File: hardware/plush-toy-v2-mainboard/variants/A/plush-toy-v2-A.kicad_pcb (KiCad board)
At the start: 4 copper layers, 52 x 46 mm, 99 parts, among them U1 ESP32-S3-WROOM-1-N16R8

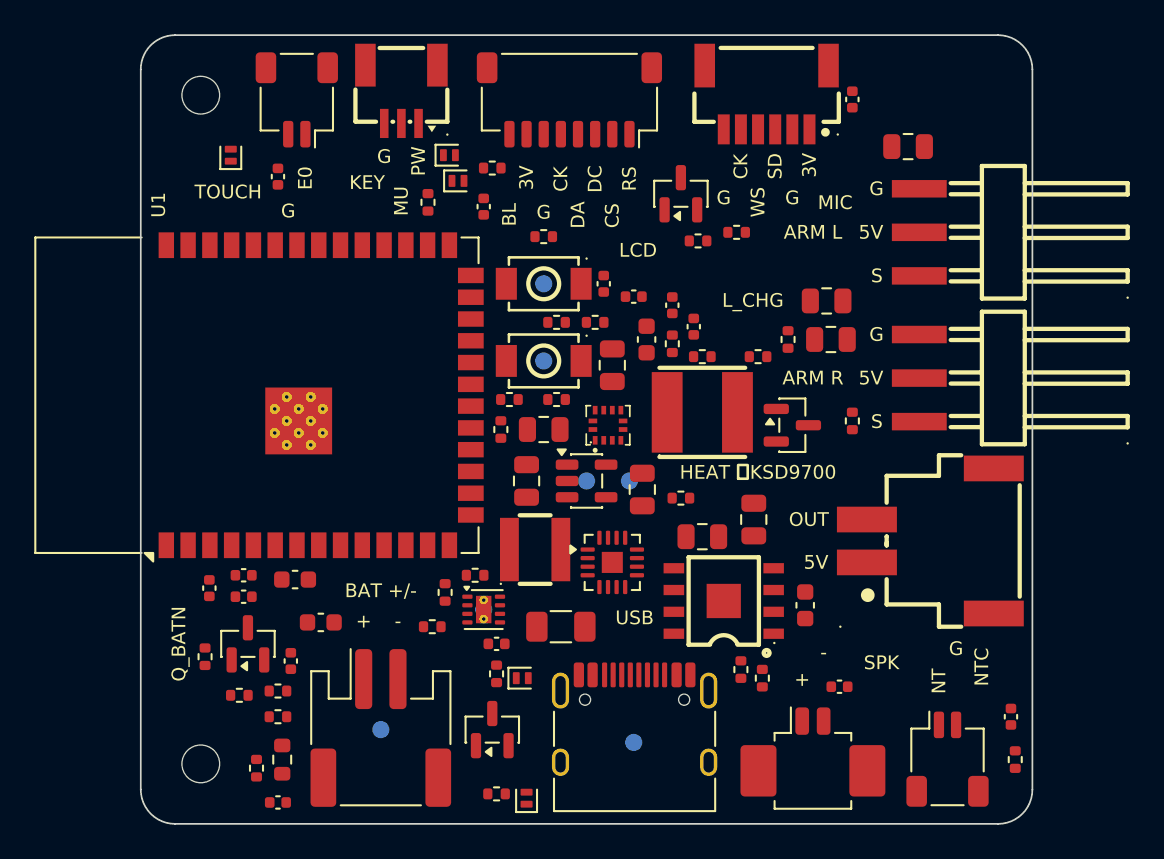
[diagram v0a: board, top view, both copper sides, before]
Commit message: feat(pcb-v2): 版本 A 布线完成，DRC 0 错误 0 未连接
- 网络类收窄（Power 0.6 / Supply 0.4 / Audio 0.3），丝印最小 0.8mm
- In2 改为 VSYS 矩形 + 其余 3V3；电源链按电流走向重排
- IMU SA0 接 3V3（0x19），降压 EN 直连 VSYS
- post_route：网格补线、拉直、快照 --from-snapshot
- route：空 SES 直接失败，非回退只比错误与未连接

Co-Authored-By: Claude Opus 5.5 <noreply@anthropic.com>
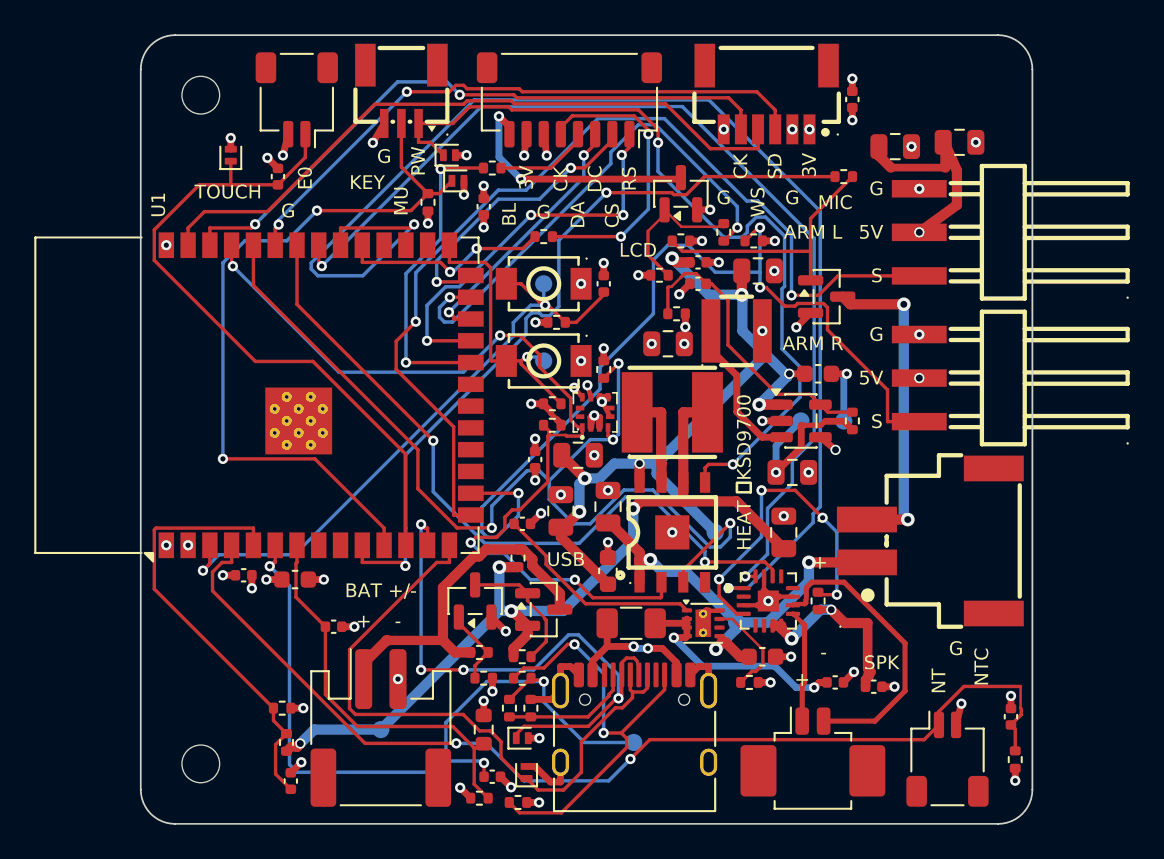
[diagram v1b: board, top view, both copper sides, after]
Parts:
- removed R_BUCK_EN: 100k, Resistor_SMD:R_0402_1005Metric
- moved C_EFUSE_IN 34.9 mm to (40.5, 37.8)
- moved C_VUSB 25.8 mm to (36.2, 36.2)
- moved R_EFUSE_ILM 20.7 mm to (35.5, 37.8), turned to 0 degrees
- moved R_FB1 20.0 mm to (41.5, 22.5), turned to 90 degrees
- moved R_FB2 19.3 mm to (31.2, 16.2)
- moved C_EFUSE_DVDT 18.6 mm to (22.2, 28.5), turned to 0 degrees
- moved L_BUCK 17.3 mm to (34.8, 17.2)
- moved R_BATN_G 16.0 mm to (19.8, 36.0), turned to 0 degrees
- moved R_AMP_SD 15.8 mm to (39.5, 33.0), turned to 90 degrees
- moved R_CC_SUM1 14.9 mm to (21.5, 39.2)
- moved TP_VUSB 14.8 mm to (34.8, 34.2)
- moved C_BUCK_OUT1 14.7 mm to (38.0, 25.5)
- moved R_BATN_PD 14.3 mm to (20.0, 37.5)
- moved Q_BATN 13.5 mm to (19.5, 33.0)
- moved R_BAT_NTC 13.1 mm to (19.8, 44.5), turned to 0 degrees
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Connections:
- J_HEAT pad 3: (no net) -> unconnected-(J_HEAT-Pad3)
- J_HEAT pad 4: (no net) -> unconnected-(J_HEAT-Pad4)
- J_KEY pad 4: (no net) -> unconnected-(J_KEY-Pad4)
- J_KEY pad 5: (no net) -> unconnected-(J_KEY-Pad5)
- J_MIC pad 7: (no net) -> unconnected-(J_MIC-Pad7)
- J_MIC pad 8: (no net) -> unconnected-(J_MIC-Pad8)
- J_USB pad A8: (no net) -> unconnected-(J_USB-SBU1-PadA8)
- J_USB pad B8: (no net) -> unconnected-(J_USB-SBU2-PadB8)
- U1 pad 17: (no net) -> unconnected-(U1-IO9-Pad17)
- U1 pad 18: (no net) -> unconnected-(U1-IO10-Pad18)
- U1 pad 19: (no net) -> unconnected-(U1-IO11-Pad19)
- U1 pad 20: (no net) -> unconnected-(U1-IO12-Pad20)
- U1 pad 21: (no net) -> unconnected-(U1-IO13-Pad21)
- U1 pad 28: (no net) -> unconnected-(U1-IO35-Pad28)
- U1 pad 29: (no net) -> unconnected-(U1-IO36-Pad29)
- U1 pad 30: (no net) -> unconnected-(U1-IO37-Pad30)
- U1 pad 8: (no net) -> unconnected-(U1-IO15-Pad8)
- U1 pad 9: (no net) -> unconnected-(U1-IO16-Pad9)
- U_AMP pad 12: (no net) -> unconnected-(U_AMP-NC-Pad12)
- U_AMP pad 13: (no net) -> unconnected-(U_AMP-NC-Pad13)
- U_AMP pad 2: (no net) -> unconnected-(U_AMP-GAIN_SLOT-Pad2)
- U_AMP pad 5: (no net) -> unconnected-(U_AMP-NC-Pad5)
- U_AMP pad 6: (no net) -> unconnected-(U_AMP-NC-Pad6)
- U_BUCK pad 1: BUCK_EN -> VSYS
- U_CHG pad 4: (no net) -> unconnected-(U_CHG-LED3-Pad4)
- U_EFUSE pad 6: (no net) -> unconnected-(U_EFUSE-FLT-Pad6)
- U_IMU pad 11: (no net) -> unconnected-(U_IMU-INT2-Pad11)
- U_IMU pad 12: (no net) -> unconnected-(U_IMU-INT1-Pad12)
- U_IMU pad 3: GND -> +3V3
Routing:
- net AMP_DIN: track 0.00 -> 75.2 mm, vias 0 -> 2
- net VSYS: track 0.00 -> 73.4 mm, vias 0 -> 12
- net NTC_SENSE: track 0.00 -> 62.0 mm, vias 0 -> 2
- net I2C_SDA: track 0.00 -> 60.7 mm, vias 0 -> 4
- net AMP_BCLK: track 0.00 -> 59.0 mm, vias 0 -> 2
- net SERVO_L_PWM: track 0.00 -> 56.9 mm, vias 0 -> 2
- net GND: track 0.00 -> 54.3 mm, vias 0 -> 58
- net I2C_SCL: track 0.00 -> 54.1 mm, vias 0 -> 4
- net SERVO_R_PWM: track 0.00 -> 53.3 mm, vias 0 -> 3
- net VBAT: track 0.00 -> 51.0 mm, vias 0 -> 4
- net KEY_PWR: track 0.00 -> 48.3 mm, vias 0 -> 2
- net CC_SENSE: track 0.00 -> 45.1 mm, vias 0 -> 3
- net HEAT_GATE_DRV: track 0.00 -> 44.9 mm, vias 0 -> 2
- net KEY_MUTE: track 0.00 -> 43.6 mm, vias 0 -> 2
- net AMP_LRCLK: track 0.00 -> 42.4 mm, vias 0 -> 2
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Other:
- board text removed: "OUT"
